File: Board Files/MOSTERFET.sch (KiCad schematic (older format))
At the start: 29 parts, among them CN11 Jumper_NC_Small, CN21 Jumper_NC_Small, J11 XT-60-M, J12 XT-60-F, J21 XT-60-M, J22 XT-60-F, Q11 AUIRFSA8409-7P, Q21 AUIRFSA8409-7P, U11 TLP182, U21 TLP182

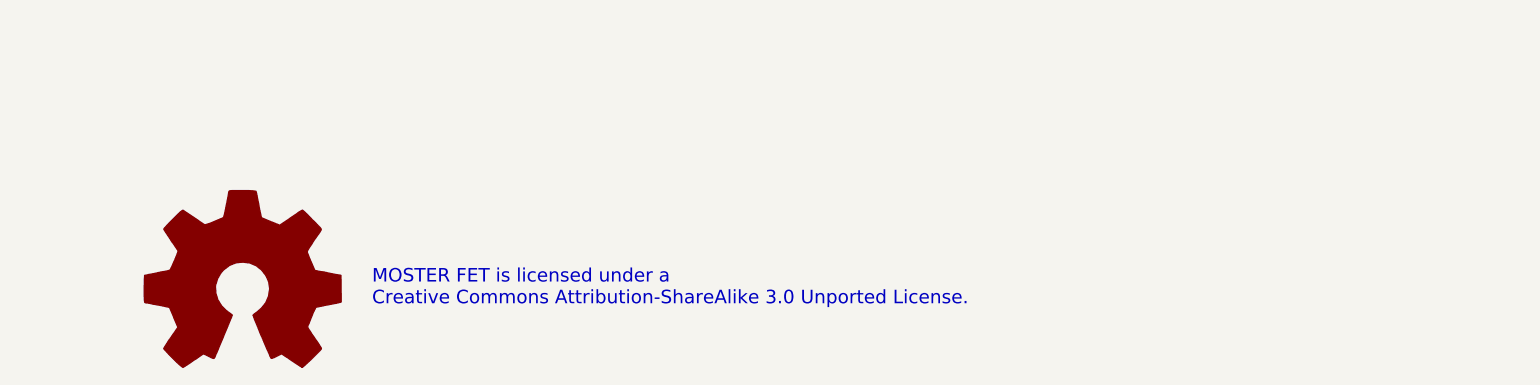
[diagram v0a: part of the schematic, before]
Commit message: Added OSHWA number to board and documents
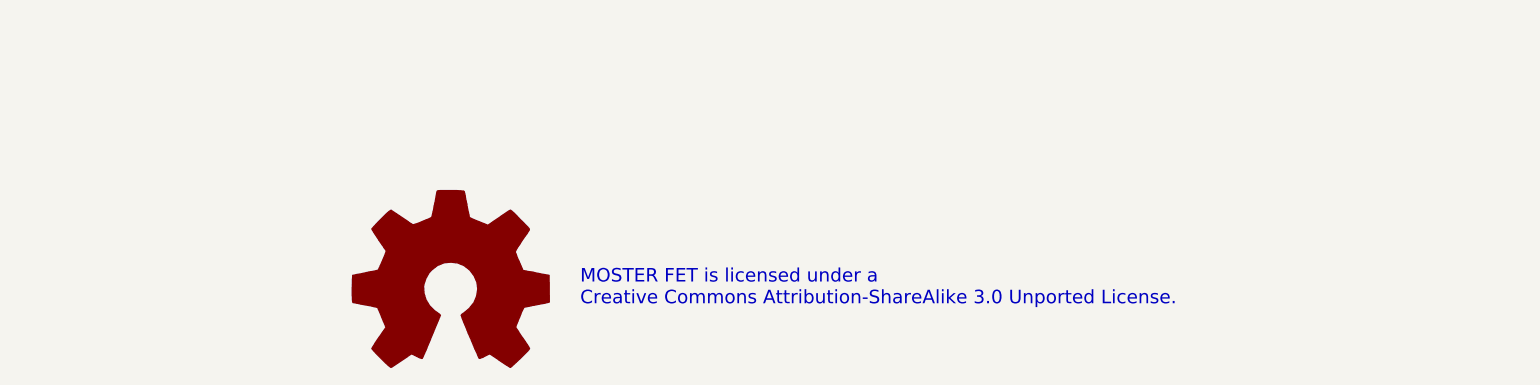
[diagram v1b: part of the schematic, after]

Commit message: LED not on placment diagrams
LED Value was ~ needed to be a part number so they showed up in the graphical bom
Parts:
- D13, D23: value ~ -> QBLP631-IW
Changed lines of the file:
@@
 P 3825 3650
 F 0 "D13" H 3775 3775 50  0000 L CNN
-F 1 "~" H 3650 3550 50  0001 L CNN
+F 1 "QBLP631-IW" H 3650 3550 50  0001 L CNN
 F 2 "LEDs:LED_0805_HandSoldering" V 3825 3650 50  0001 C CNN
 F 3 "http://www.qt-brightek.com/datasheet/QBLP631_series.pdf" V 3825 3650 50  0001 C CNN
@@
 P 7925 3725
 F 0 "D23" H 7875 3850 50  0000 L CNN
-F 1 "~" H 7750 3625 50  0001 L CNN
+F 1 "QBLP631-IW" H 7750 3625 50  0001 L CNN
 F 2 "LEDs:LED_0805_HandSoldering" V 7925 3725 50  0001 C CNN
 F 3 "http://www.qt-brightek.com/datasheet/QBLP631_series.pdf" V 7925 3725 50  0001 C CNN

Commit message: Moved components for better diode soldering
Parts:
- CN11, CN21, J11, J12, J21, J22: symbol conn:CONN_01X02 -> Connector_Generic:Conn_01x02
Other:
- moved on the sheet: C11, C21, D11, D13, D21, D23, Q11, Q21, R11, R12, R13, R15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
